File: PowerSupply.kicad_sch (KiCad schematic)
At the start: 20 parts, among them U1 MIC2288YD5-TR, U3 MIC2288YD5-TR

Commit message: Annotations
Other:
- note added: "R1, 2, 3, and 4 control the output voltages of the power supply."
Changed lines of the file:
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@@
     (stroke (width 0) (type default))
+  )
+  (text "R1, 2, 3, and 4 control the output \nvoltages of the power supply."
+    (at 194.31 86.995 0)
+    (effects (font (size 1.27 1.27)) (justify left bottom))
   )
   (hierarchical_label "18V" (shape bidirectional) (at 180.975 56.515 0) (fields_autoplaced)

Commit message: Components on PCB, all warnings and error fixed
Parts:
- U1, U3: footprint MIC2288YD5-TR:SOT95P280X100-5N -> Proj:SOT95P280X100-5N
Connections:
- net 18V: now also D1.2 (C), TP1.TP (1); no longer D1.1 (K), TP1.1
- net 3.3V: now also TP3.TP (1); no longer TP3.1
- net GND: now also TP2.TP (1); no longer TP2.1
- net at BT1.1 (+), MOSFET2.3: now also TP4.TP; no longer TP4.1
- net at L1.2, U1.1 (SW): now also D1.1 (A); no longer D1.2 (A)
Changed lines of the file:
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@@
     (effects (font (size 1.27 1.27)) (justify left))
   )
-  (symbol (lib_id "Connector:TestPoint") (at 76.835 56.515 0) (unit 1)
+  (symbol (lib_name "TestPoint_1") (lib_id "Connector:TestPoint") (at 76.835 56.515 0) (unit 1)
     (in_bom yes) (on_board yes) (dnp no) (fields_autoplaced)
     (property "Reference" "TP4" (at 78.74 51.943 0)
@@
       (effects (font (size 1.27 1.27)) hide)
     )
-    (pin "1")
+    (pin "TP")
     (instances
       (project "CatLasers"
@@
     )
   )
-  (symbol (lib_id "Hestres_Standard_Lib:D_Schottky") (at 156.21 56.515 0) (mirror y) (unit 1)
+  (symbol (lib_name "D_Schottky_1") (lib_id "Hestres_Standard_Lib:D_Schottky") (at 156.21 56.515 0) (mirror y) (unit 1)
     (in_bom yes) (on_board yes) (dnp no)
     (property "Reference" "D1" (at 156.21 53.34 0)
@@
       (effects (font (size 1.27 1.27)) hide)
     )
-    (property "Footprint" "Proj:SODFL3618X110N" (at 156.21 56.515 0)
+    (property "Footprint" "Proj:SODFL3618X110N" (at 156.21 59.69 0)
       (effects (font (size 1.27 1.27)) hide)
     )
@@
       (effects (font (size 1.27 1.27)) hide)
     )
-    (pin "1")
-    (pin "2")
+    (pin "2")
+    (pin "1")
     (instances
       (project "CatLasers"
@@
       (effects (font (size 1.27 1.27)))
     )
-    (property "Footprint" "MIC2288YD5-TR:SOT95P280X100-5N" (at 134.62 99.06 0)
+    (property "Footprint" "Proj:SOT95P280X100-5N" (at 134.62 99.06 0)
       (effects (font (size 1.27 1.27)) (justify bottom) hide)
     )
@@
       (effects (font (size 1.27 1.27)) hide)
     )
-    (pin "1")
+    (pin "TP")
     (instances
       (project "CatLasers"
@@
     )
   )
-  (symbol (lib_id "Connector:TestPoint") (at 177.165 86.36 0) (unit 1)
+  (symbol (lib_name "TestPoint_3") (lib_id "Connector:TestPoint") (at 177.165 86.36 0) (unit 1)
     (in_bom yes) (on_board yes) (dnp no)
     (property "Reference" "TP2" (at 179.07 81.788 0)
@@
       (effects (font (size 1.27 1.27)) hide)
     )
-    (pin "1")
+    (pin "TP")
     (instances
       (project "CatLasers"
@@
     )
   )
-  (symbol (lib_id "Connector:TestPoint") (at 177.165 56.515 0) (unit 1)
+  (symbol (lib_name "TestPoint_2") (lib_id "Connector:TestPoint") (at 177.165 56.515 0) (unit 1)
     (in_bom yes) (on_board yes) (dnp no)
     (property "Reference" "TP1" (at 179.07 51.943 0)
@@
       (effects (font (size 1.27 1.27)) hide)
     )
-    (pin "1")
+    (pin "TP")
     (instances
       (project "CatLasers"
@@
       (effects (font (size 1.27 1.27)))
     )
-    (property "Footprint" "MIC2288YD5-TR:SOT95P280X100-5N" (at 134.62 73.66 0)
-      (effects (font (size 1.27 1.27)) (justify bottom) hide)
-    )
+    (property "Footprint" "Proj:SOT95P280X100-5N" (at 134.62 73.66 0)
+      (effects (font (size 1.27 1.27)) (justify bottom) hide)
+    )

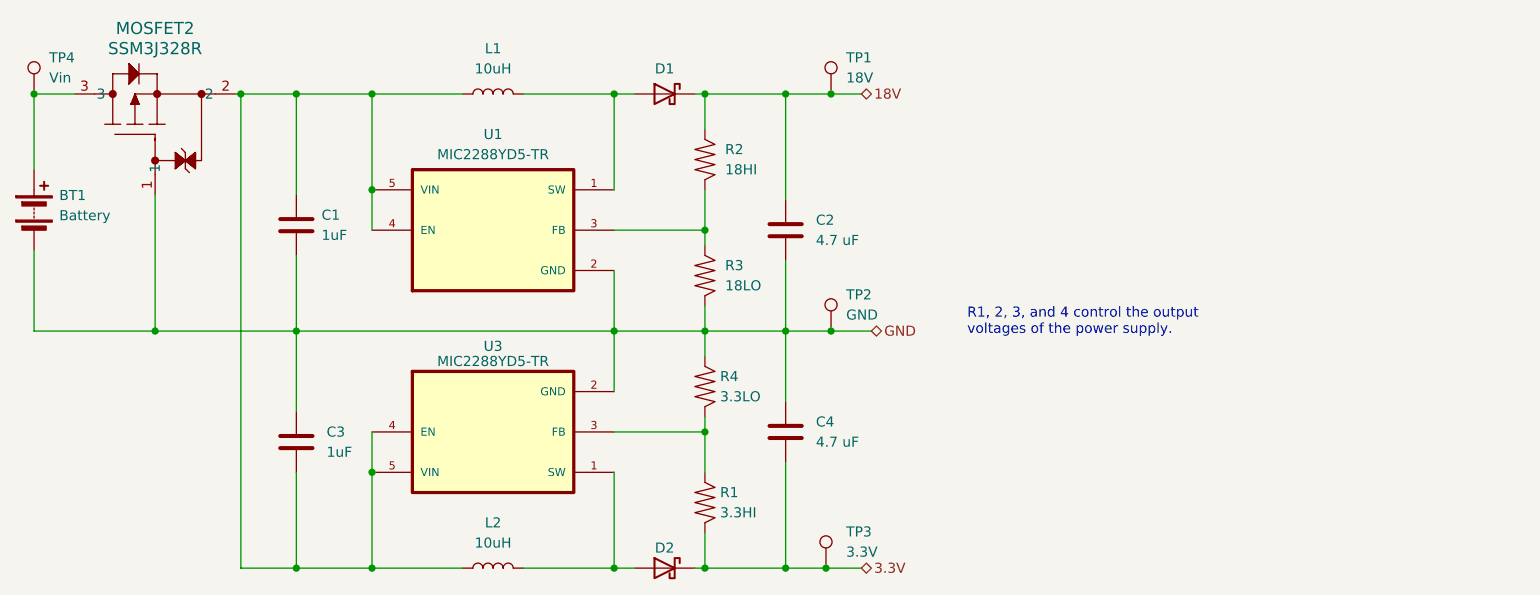
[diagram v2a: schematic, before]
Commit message: Added Voltage stabalizing capacitors
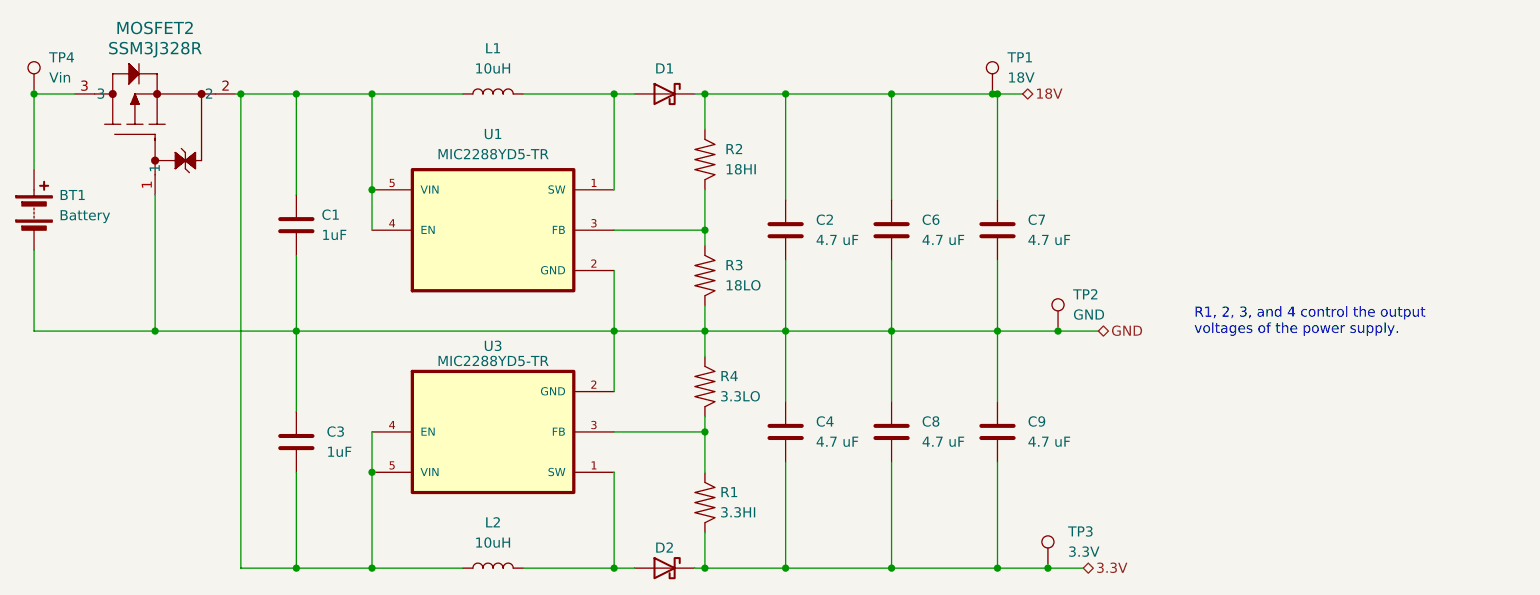
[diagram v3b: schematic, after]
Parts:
- added C6, C7, C8, C9: 4.7 uF, Capacitor_SMD:C_0805_2012Metric, symbol Hestres_Standard_Lib:C
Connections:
- net 18V: now also C6.1, C7.1
- net 3.3V: now also C8.2, C9.2
- net GND: now also C6.2, C7.2, C8.1, C9.1
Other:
- moved on the sheet: TP1, TP2, TP3

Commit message: Revert "Added Voltage stabalizing capacitors"
This reverts commit 707a44219213f2b52e07c81fee0218c85384a0bb.
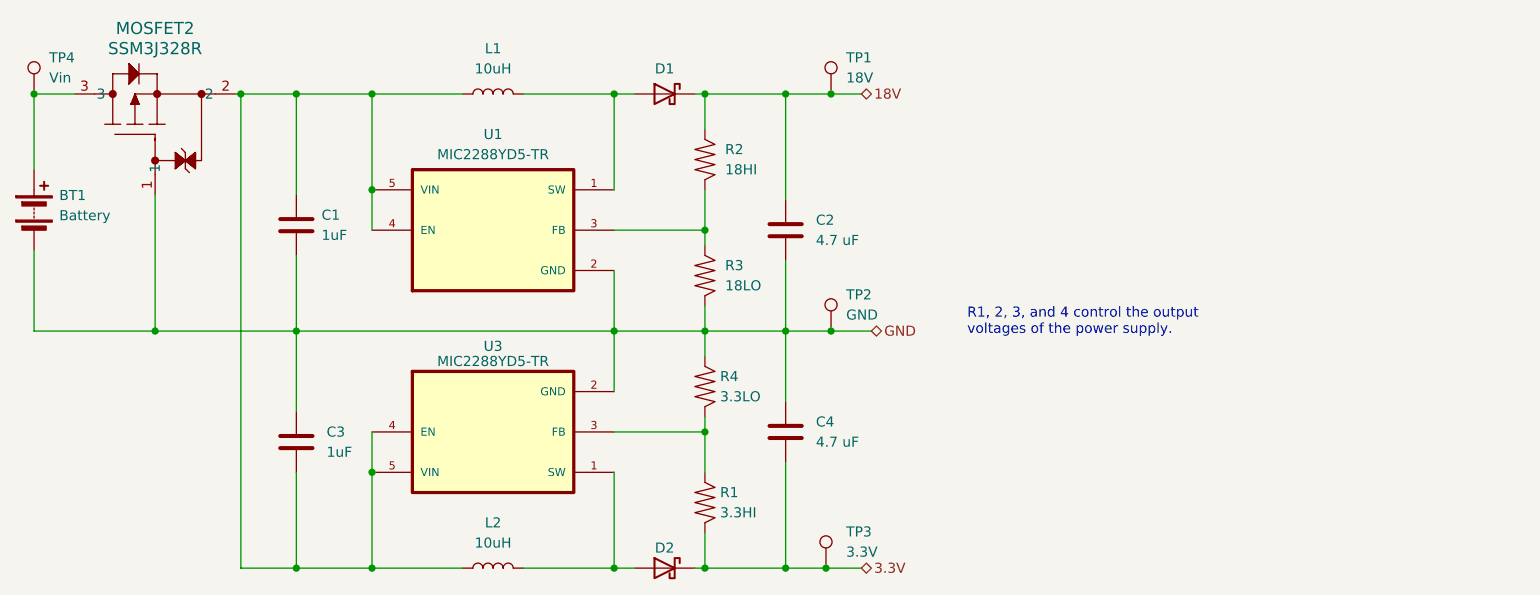
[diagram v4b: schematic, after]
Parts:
- removed C6, C7, C8, C9: 4.7 uF, Capacitor_SMD:C_0805_2012Metric, symbol Hestres_Standard_Lib:C
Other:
- moved on the sheet: TP1, TP2, TP3

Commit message: Power Supply Net Labels
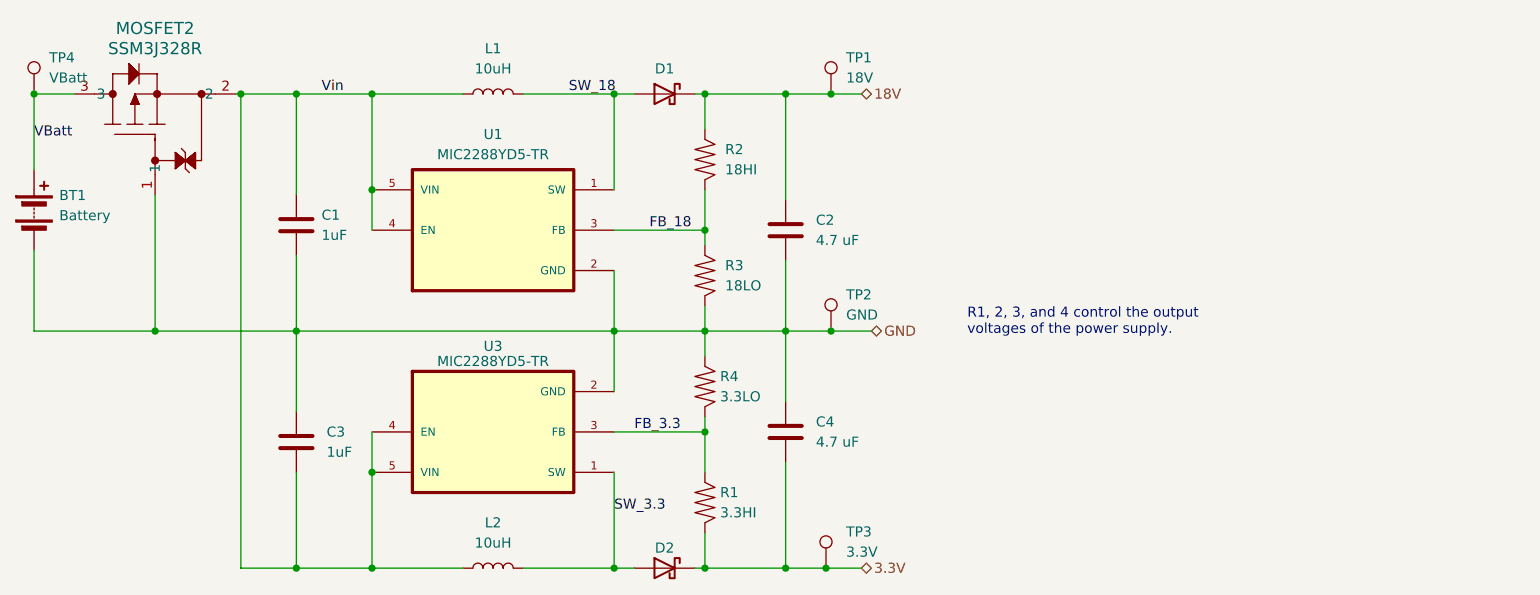
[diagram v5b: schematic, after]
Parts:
- TP4: value Vin -> VBatt
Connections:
- net VBatt: now reaches BT1.1 (+), MOSFET2.3, TP4.TP
- net SW_18: now reaches D1.1 (A), L1.2, U1.1 (SW)
- net SW_3.3: now reaches D2.2 (A), L2.2, U3.1 (SW)
- net FB_3.3: now reaches R1.1, R4.2, U3.3 (FB)
- net Vin: now reaches C1.1, C3.2, L1.1, L2.1, MOSFET2.2, U1.4 (EN), U1.5 (VIN), U3.4 (EN), U3.5 (VIN)
- net FB_18: now reaches R2.2, R3.1, U1.3 (FB)
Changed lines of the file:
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@@
+    (effects (font (size 1.27 1.27)) (justify left bottom))
+  )
+  (label "FB_18" (at 154.305 73.66 0) (fields_autoplaced)
+    (effects (font (size 1.27 1.27)) (justify left bottom))
+  )
+  (label "Vin" (at 113.03 56.515 0) (fields_autoplaced)
+    (effects (font (size 1.27 1.27)) (justify left bottom))
+  )
+  (label "SW_18" (at 144.145 56.515 0) (fields_autoplaced)
+    (effects (font (size 1.27 1.27)) (justify left bottom))
+  )
+  (label "VBatt" (at 76.835 62.23 0) (fields_autoplaced)
+    (effects (font (size 1.27 1.27)) (justify left bottom))
+  )
+  (label "SW_3.3" (at 149.86 109.22 0) (fields_autoplaced)
+    (effects (font (size 1.27 1.27)) (justify left bottom))
+  )
+  (label "FB_3.3" (at 152.4 99.06 0) (fields_autoplaced)
     (effects (font (size 1.27 1.27)) (justify left bottom))
   )
@@
       (effects (font (size 1.27 1.27)) (justify left))
     )
-    (property "Value" "Vin" (at 78.74 54.483 0)
+    (property "Value" "VBatt" (at 78.74 54.483 0)
       (effects (font (size 1.27 1.27)) (justify left))
     )
@@
       (effects (font (size 1.27 1.27)) hide)
     )
+    (pin "1")
     (pin "2")
-    (pin "1")
     (instances
       (project "CatLasers"

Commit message: Piezzo Layout
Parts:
- renumbered MOSFET2 to FET2
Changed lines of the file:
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@@
   )
   (symbol (lib_id "ProjPMOS_LV:SSM3J328R") (at 84.455 66.675 90) (unit 1)
-    (in_bom yes) (on_board yes) (dnp no) (fields_autoplaced)
-    (property "Reference" "MOSFET2" (at 92.075 48.26 90)
+    (in_bom yes) (on_board yes) (dnp no)
+    (property "Reference" "FET2" (at 90.805 50.8 90)
       (effects (font (size 1.524 1.524)))
     )
     (property "Value" "SSM3J328R" (at 92.075 50.8 90)
-      (effects (font (size 1.524 1.524)))
+      (effects (font (size 1.524 1.524)) hide)
     )
     (property "Footprint" "Proj:SOT-23F_TOS" (at 84.455 66.675 0)
@@
       (project "CatLasers"
         (path "/b94f5b10-ee0c-4425-b025-e3a8bb3cc7b0/af549741-ba89-4808-a98f-faa5cfb79fa3"
-          (reference "MOSFET2") (unit 1)
+          (reference "FET2") (unit 1)
         )
       )
